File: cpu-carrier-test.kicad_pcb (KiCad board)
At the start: 2 copper layers, 64.3 x 60.8 mm, 44 parts, among them J19 SFP, J20 SFP_CAGE, J4 JTAG, J5 Molex_0936263508, J6 USB_A, J98 Conn_02x06_Top_Bottom, J99 Conn_02x06_Top_Bottom, SW1 SW_Push, U6 PCA9546AD, U8 74AC125, U9 TPS2051B

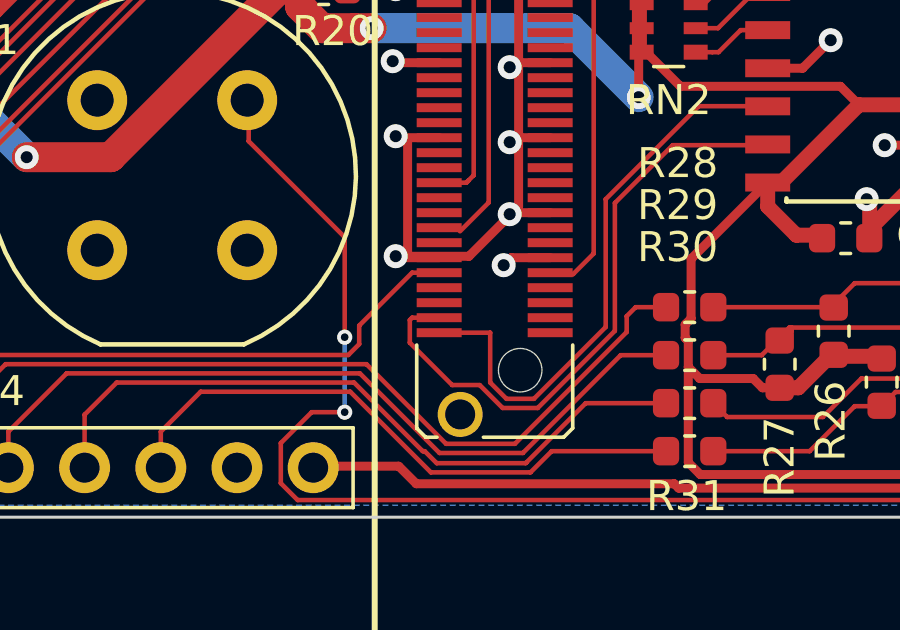
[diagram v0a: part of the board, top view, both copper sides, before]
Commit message: re-routed i2c from mio12/13 -> mio10/11 on PCB
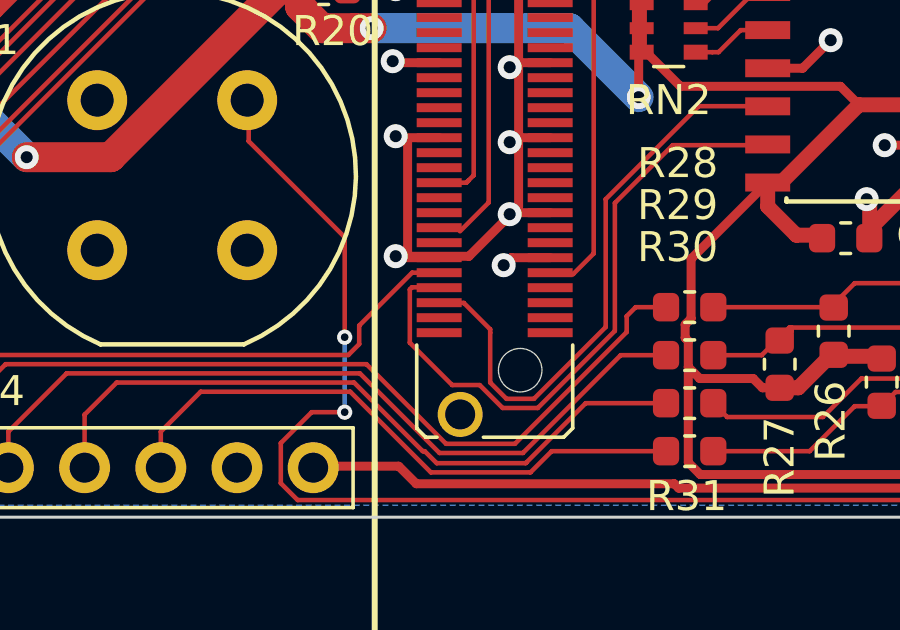
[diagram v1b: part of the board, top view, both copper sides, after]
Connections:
- JB1 pad 100: SCLK_MIO12 -> /B2B Connector/MIO12
- JB1 pad 94: /B2B Connector/MIO11 -> SDA_MIO11
- JB1 pad 96: /B2B Connector/MIO10 -> SCLK_MIO10
- JB1 pad 98: SDA_MIO13 -> /B2B Connector/MIO13
- U6 pad 14: SCLK_MIO12 -> SCLK_MIO10
- U6 pad 15: SDA_MIO13 -> SDA_MIO11
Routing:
- net SDA_MIO11: track 0.00 -> 21.8 mm
- net SDA_MIO13: track 20.7 -> 0.00 mm
- net SCLK_MIO10: track 0.00 -> 19.9 mm
- net SCLK_MIO12: track 19.4 -> 0.00 mm

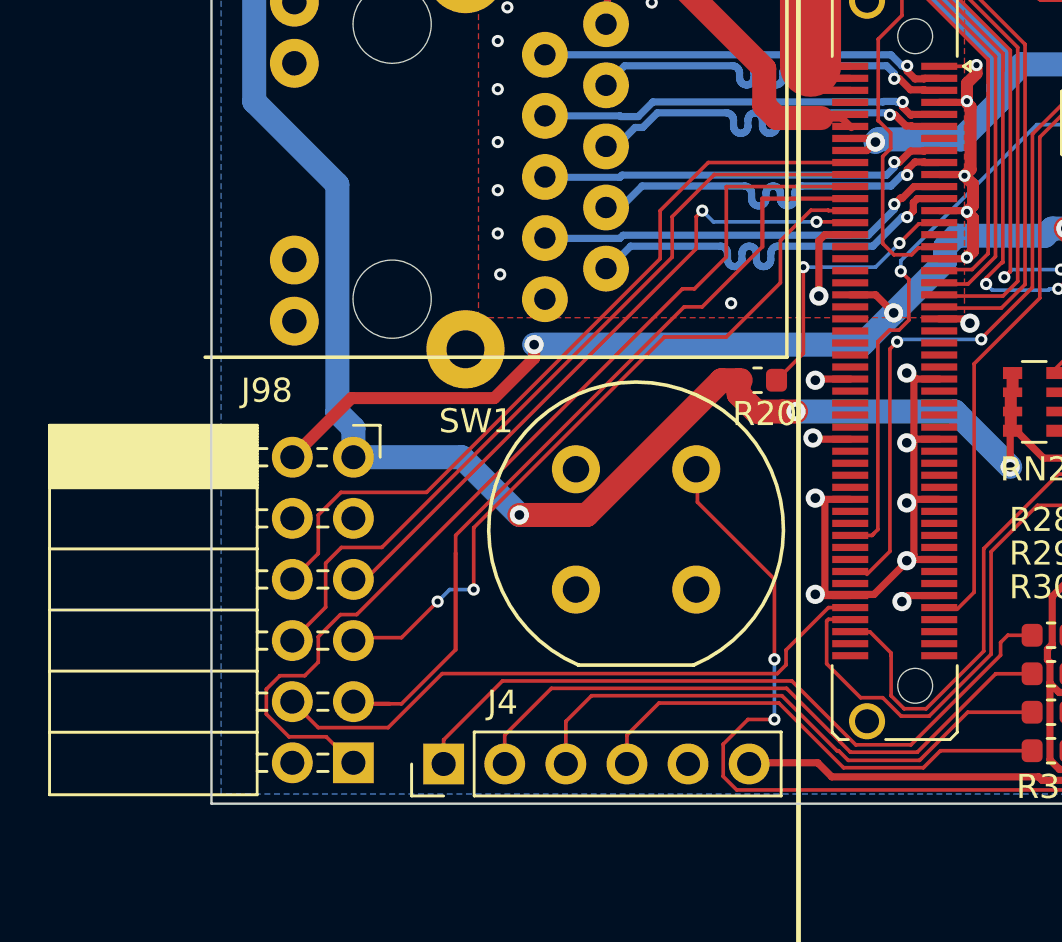
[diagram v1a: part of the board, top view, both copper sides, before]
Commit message: hooked up SD-card; use smaller reset button
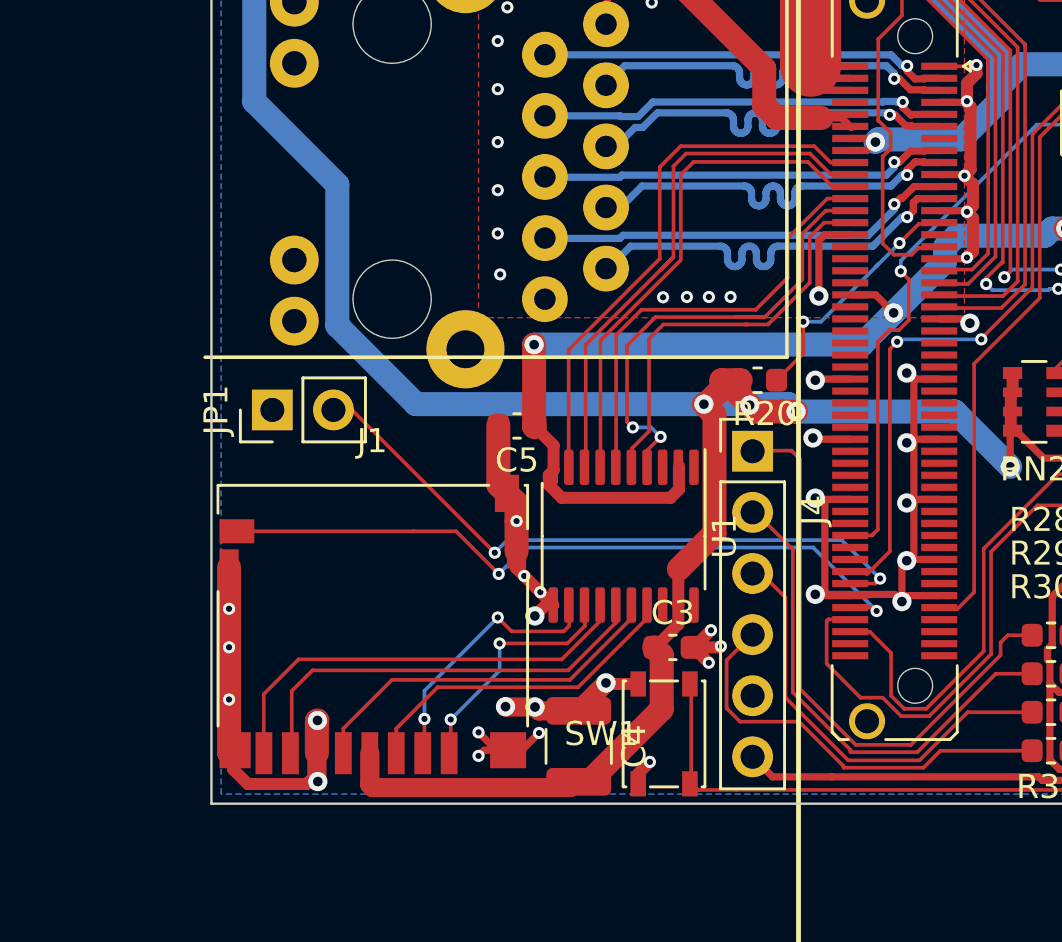
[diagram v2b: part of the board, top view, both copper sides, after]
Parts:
- removed J98: Conn_02x06_Top_Bottom, pmod:PinSocket_2x06_P2.54mm_Horizontal
- added C3: 100nF_603, Capacitor_SMD:C_0603_1608Metric, F.Cu at (131.8, 87.9)
- added C4: 10uF_1210, Capacitor_SMD:C_1210_3225Metric, F.Cu at (127.9, 92.0)
- added C5: 100nF_603, Capacitor_SMD:C_0603_1608Metric, F.Cu at (125.3, 78.7)
- added J1: Micro_SD_Card_Det, Connector_Card:microSD_HC_Hirose_DM3D-SF, F.Cu at (119.3, 87.0)
- added JP1: Jumper_NO_Small, Connector_PinHeader_2.54mm:PinHeader_1x02_P2.54mm_Vertical, F.Cu at (115.1, 78.0)
- added U1: TXS0108EPW, Package_SO:TSSOP-20_4.4x6.5mm_P0.65mm, F.Cu at (129.7, 83.3)
- SW1: footprint Button_Switch_THT:Push_E-Switch_KS01Q01 -> Button_Switch_SMD:SW_SPST_PTS810
- moved J4 18.3 mm to (135.1, 79.8), turned to 0 degrees
- moved SW1 11.6 mm to (131.4, 91.5), turned to 90 degrees
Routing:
- net OTG_ID: track 181.5 -> 222.3 mm, vias 71 -> 93
- net +3V3: track 227.7 -> 255.3 mm, vias 10 -> 11
- net MIO_0: track 0.00 -> 26.6 mm, vias 0 -> 2
- net SD0_D1_MIO43: track 41.0 -> 21.3 mm
- net Net-(J1-Pad8): track 0.00 -> 18.4 mm
- net Net-(J1-Pad7): track 0.00 -> 17.9 mm
- net Net-(J1-Pad5): track 0.00 -> 15.7 mm
- net SD0_D0_MIO42: track 33.4 -> 18.8 mm
- net Net-(J1-Pad3): track 0.00 -> 14.0 mm
- net SD0_D2_MIO44: track 33.7 -> 22.8 mm
- net Net-(J1-Pad2): track 0.00 -> 10.9 mm, vias 0 -> 2
- net /B2B Connector/RESIN: track 82.9 -> 72.6 mm, vias 2 -> 0
- net SD0_CMD_MIO41: track 30.5 -> 20.3 mm
- net SD0_CLK_MIO40: track 27.6 -> 17.5 mm, vias 2 -> 0
- net Net-(J1-Pad1): track 0.00 -> 9.93 mm, vias 0 -> 2
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
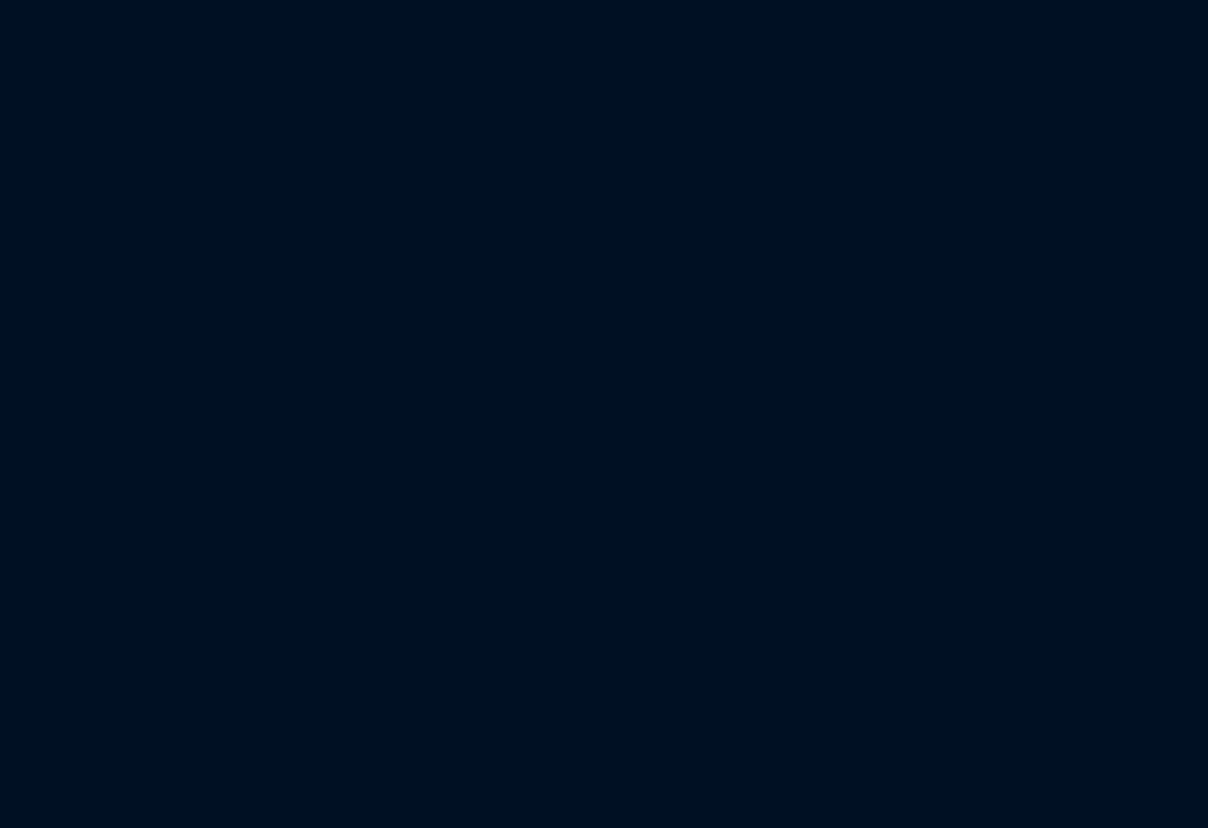
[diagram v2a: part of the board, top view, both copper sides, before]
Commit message: merged power-test sub-PCB
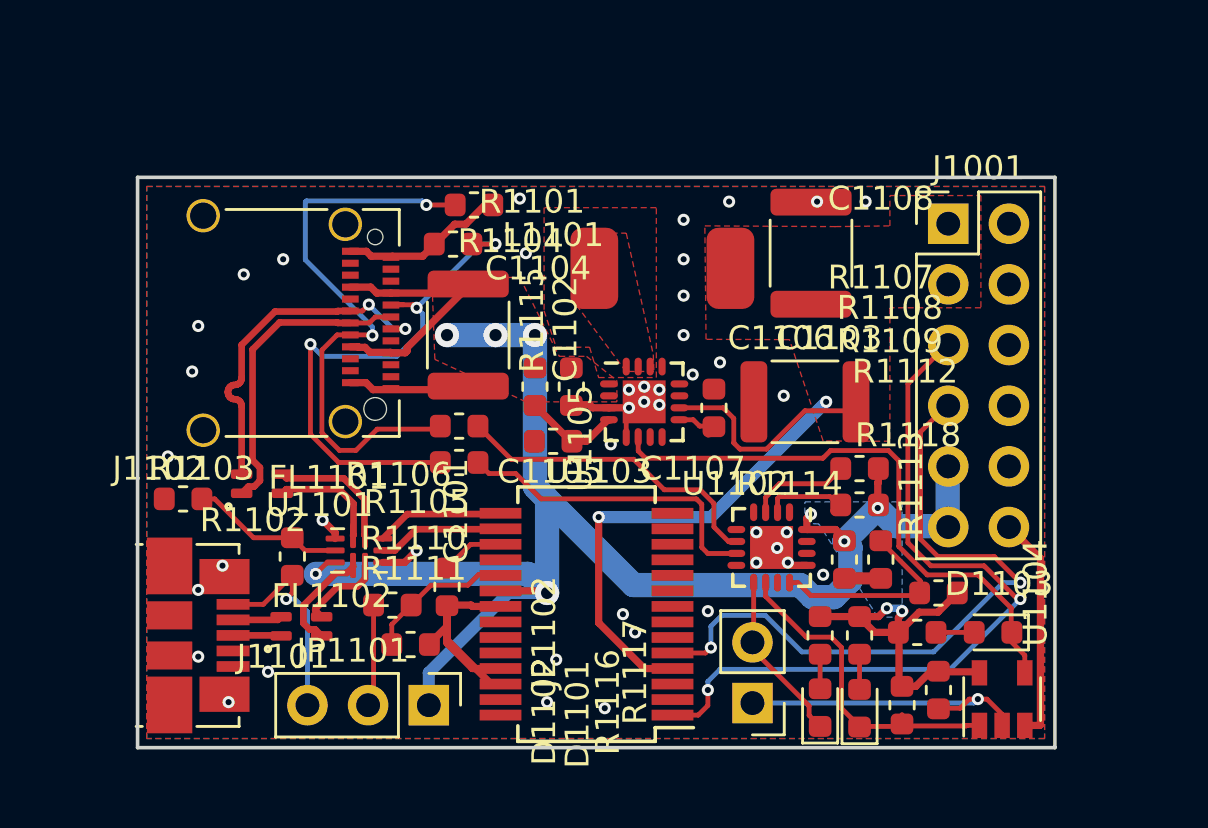
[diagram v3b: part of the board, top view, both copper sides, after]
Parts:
- added C1101: 100nF_603, Capacitor_SMD:C_0603_1608Metric, F.Cu at (126.2, 130.2)
- added C1102: 100nF_603, Capacitor_SMD:C_0603_1608Metric, F.Cu at (131.4, 121.8)
- added C1103: 100nF_603, Capacitor_SMD:C_0603_1608Metric, F.Cu at (142.9, 129.0)
- added C1104: 22uF_lo_ESR, Capacitor_SMD:C_1812_4532Metric, F.Cu at (127.1, 119.6)
- added C1105: 100nF_603, Capacitor_SMD:C_0603_1608Metric, F.Cu at (130.7, 124.1)
- added C1106: 22uF_lo_ESR, Capacitor_SMD:C_1812_4532Metric, F.Cu at (141.2, 122.4)
- added C1107: 100nF_603, Capacitor_SMD:C_0603_1608Metric, F.Cu at (137.4, 122.7)
- added C1108: 22uF_lo_ESR, Capacitor_SMD:C_1812_4532Metric, F.Cu at (141.5, 116.2)
- added D1101: LED, LED_SMD:LED_0603_1608Metric, F.Cu at (143.5, 135.3)
- added D1102: LED, LED_SMD:LED_0603_1608Metric, F.Cu at (141.9, 135.2)
- added D1103: LED, LED_SMD:LED_0603_1608Metric, F.Cu at (149.1, 132.1)
- added FL1101: EMI_Filter_LL_14, proj_footprints:WE_CNSW, F.Cu at (118.5, 125.9)
- added FL1102: EMI_Filter_LL_14, proj_footprints:WE_CNSW, F.Cu at (120.1, 131.8)
- added J1001: Conn_02x06_Odd_Even, Connector_PinHeader_2.54mm:PinHeader_2x06_P2.54mm_Vertical, F.Cu at (147.2, 115.0)
- added J1101: USB_miniB, Connector_USB:USB_Micro-B_Molex_47346-0001, F.Cu at (115.8, 132.2)
- added J1102: USB_C_Receptacle, Connector_USB:USB_C_Receptacle_Amphenol_12401610E4-2A_CircularHoles, F.Cu at (118.9, 119.1)
- added JP1101: Jumper_3_Bridged12, Connector_PinHeader_2.54mm:PinHeader_1x03_P2.54mm_Vertical, F.Cu at (125.5, 135.1)
- added JP1102: Jumper_NO_Small, Connector_PinHeader_2.54mm:PinHeader_1x02_P2.54mm_Vertical, F.Cu at (139.0, 135.0)
- added L1101: 1uH, proj_footprints:L_CDMC6D28, F.Cu at (135.3, 116.8)
- added R1101: 5k1, Resistor_SMD:R_0603_1608Metric, F.Cu at (127.4, 114.2)
- added R1102: R100k, Resistor_SMD:R_0603_1608Metric, F.Cu at (119.8, 128.9)
- added R1103: R100k, Resistor_SMD:R_0603_1608Metric, F.Cu at (115.2, 126.5)
- added R1104: 5k1, Resistor_SMD:R_0603_1608Metric, F.Cu at (126.5, 115.8)
- added R1105: R10k, Resistor_SMD:R_0603_1608Metric, F.Cu at (126.7, 125.0)
- added R1106: R10k, Resistor_SMD:R_0603_1608Metric, F.Cu at (126.7, 123.4)
- added R1107: R10k, Resistor_SMD:R_0603_1608Metric, F.Cu at (143.5, 125.2)
- added R1108: R10k, Resistor_SMD:R_0603_1608Metric, F.Cu at (143.5, 126.7)
- added R1109: 5k1, Resistor_SMD:R_0603_1608Metric, F.Cu at (144.4, 129.0)
- added R1110: R4k7, Resistor_SMD:R_0603_1608Metric, F.Cu at (124.0, 130.9)
- added R1111: R10k, Resistor_SMD:R_0603_1608Metric, F.Cu at (124.7, 132.6)
- added R1112: 35k7, Resistor_SMD:R_0603_1608Metric, F.Cu at (146.8, 130.4)
- added R1113: 1k5, Resistor_SMD:R_0603_1608Metric, F.Cu at (143.5, 132.2)
- added R1114: 1k5, Resistor_SMD:R_0603_1608Metric, F.Cu at (141.9, 132.2)
- added R1115: 1, Resistor_SMD:R_0603_1608Metric, F.Cu at (129.9, 121.8)
- added R1116: R100k, Resistor_SMD:R_0603_1608Metric, F.Cu at (145.3, 135.1)
- added R1117: R100k, Resistor_SMD:R_0603_1608Metric, F.Cu at (146.8, 134.5)
- added R1118: 1k5, Resistor_SMD:R_0603_1608Metric, F.Cu at (145.9, 132.1)
- added U1101: USB3740B-AI9, Package_DFN_QFN:UQFN-10_1.6x2.1mm_P0.5mm, F.Cu at (122.6, 128.7)
- added U1102: UTC2000, proj_footprints:QFN-16-1EP_3x3mm_P0.5mm_EP1.8x1.8mm, F.Cu at (139.8, 128.5)
- added U1103: FT232RL, Package_SO:SSOP-28_5.3x10.2mm_P0.65mm, F.Cu at (132.1, 131.3)
- added U1104: 74LVC1G00, Package_TO_SOT_SMD:SOT-23-5, F.Cu at (149.5, 134.9)
- added U1105: SC185, proj_footprints:QFN-16-1EP_3x3mm_P0.5mm_EP1.8x1.8mm, F.Cu at (134.5, 122.4)
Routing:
- net Net-(C14-Pad1): track 12.4 -> 102.9 mm, vias 0 -> 10
- net Net-(FL3-Pad3): track 14.6 -> 59.8 mm, vias 0 -> 43
- net PHY_MDIO0_N: track 17.0 -> 48.9 mm, vias 1 -> 3
- net PHY_MDIO1_N: track 17.0 -> 46.4 mm, vias 1 -> 3
- net PHY_MDIO1_P: track 17.1 -> 45.7 mm, vias 1 -> 3
- net SCL1: track 54.5 -> 79.2 mm, vias 2 -> 4
- net SD0_D2_MIO44: track 22.8 -> 46.8 mm
- net UART_TX_MIO15: track 67.6 -> 90.8 mm, vias 2 -> 5
- net PHY_MDIO2_N: track 17.0 -> 31.6 mm, vias 1 -> 3
- net +3V3: track 255.3 -> 269.2 mm
- net MGT_TX1_N: track 37.0 -> 50.5 mm
- net SDA3: track 2.94 -> 16.4 mm
- net Net-(C59-Pad1): track 16.9 -> 30.0 mm, vias 2 -> 3
- net PHY_MDIO2_P: track 17.2 -> 30.2 mm
- net SD0_D0_MIO42: track 18.8 -> 27.9 mm, vias 0 -> 1
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- added copper zone on B.Cu, net +5V
- added copper zone on F.Cu, net +5V
- added copper zone on B.Cu, net GND
- added copper zone on F.Cu, net GND
- added copper zone on F.Cu, net Net-(L1101-Pad2)
- added copper zone on F.Cu, net VIN_3V3
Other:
- board size 64.3 x 60.8 mm -> 64.3 x 103.3 mm
